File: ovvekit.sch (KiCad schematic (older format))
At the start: 29 parts, among them J1 ESP_PROG_JTAG, J2 ESP_PROG_UART, SW1 SW_Push, SW2 SW_Push, SW3 SW_Push, U1 ESP32-WROOM-32

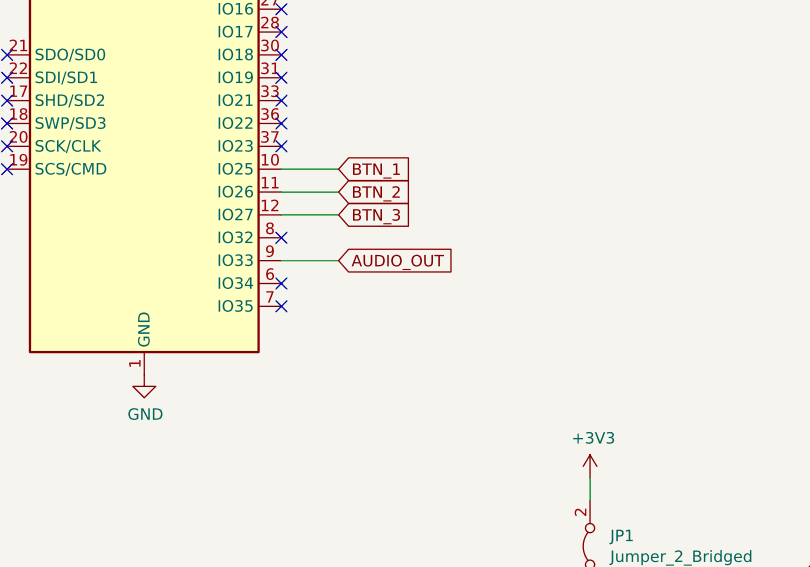
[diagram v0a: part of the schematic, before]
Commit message: Added a LDO, maybe not the final one but there is one on the PCB now. Added a voltage divider for measureing battery voltage.
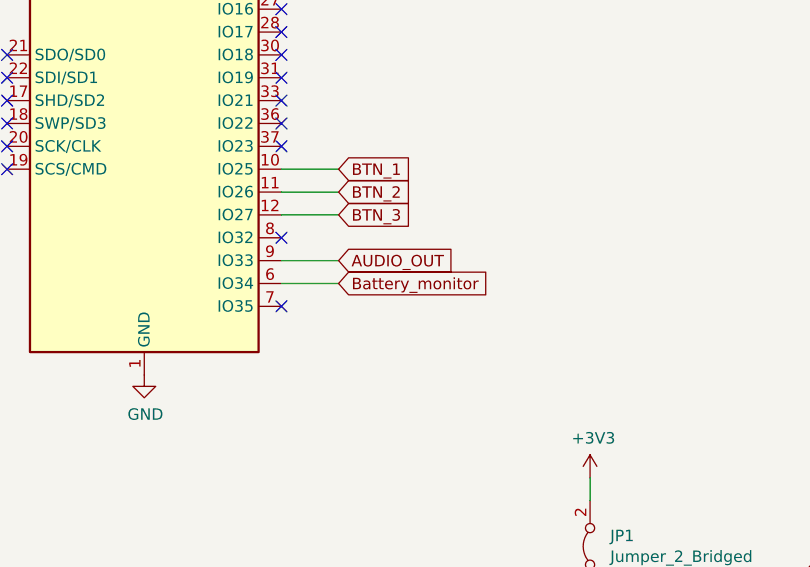
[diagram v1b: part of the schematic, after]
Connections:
- net Battery_monitor: now reaches U1.6 (IO34)
- no-connect marks 21 -> 20
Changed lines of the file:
@@
 Comment4 ""
 $EndDescr
-$Comp
-L RF_Module:ESP32-WROOM-32 U1
-U 1 1 6063995A
-P 4050 3200
-F 0 "U1" H 4050 4781 50  0000 C CNN
-F 1 "ESP32-WROOM-32" H 4050 4690 50  0000 C CNN
-F 2 "RF_Module:ESP32-WROOM-32" H 4050 1700 50  0001 C CNN
-F 3 "https://www.espressif.com/sites/default/files/documentation/esp32-wroom-32_datasheet_en.pdf" H 3750 3250 50  0001 C CNN
-	1    4050 3200
-	1    0    0    -1
-$EndComp
 Wire Wire Line
 	4900 3700 4650 3700
@@
 NoConn ~ 3450 3700
 NoConn ~ 4650 4300
-NoConn ~ 4650 4200
 NoConn ~ 4650 4000
 NoConn ~ 4650 3600
@@
 Wire Wire Line
 	6000 5150 6000 5050
+$Comp
+L RF_Module:ESP32-WROOM-32 U1
+U 1 1 6063995A
+P 4050 3200
+F 0 "U1" H 4050 4781 50  0000 C CNN
+F 1 "ESP32-WROOM-32" H 4050 4690 50  0000 C CNN
+F 2 "RF_Module:ESP32-WROOM-32" H 4050 1700 50  0001 C CNN
+F 3 "https://www.espressif.com/sites/default/files/documentation/esp32-wroom-32_datasheet_en.pdf" H 3750 3250 50  0001 C CNN
+	1    4050 3200
+	1    0    0    -1
+$EndComp
+Wire Wire Line
+	4900 4200 4650 4200
+Text GLabel 4900 4200 2    50   Input ~ 0
+Battery_monitor
 $EndSCHEMATC

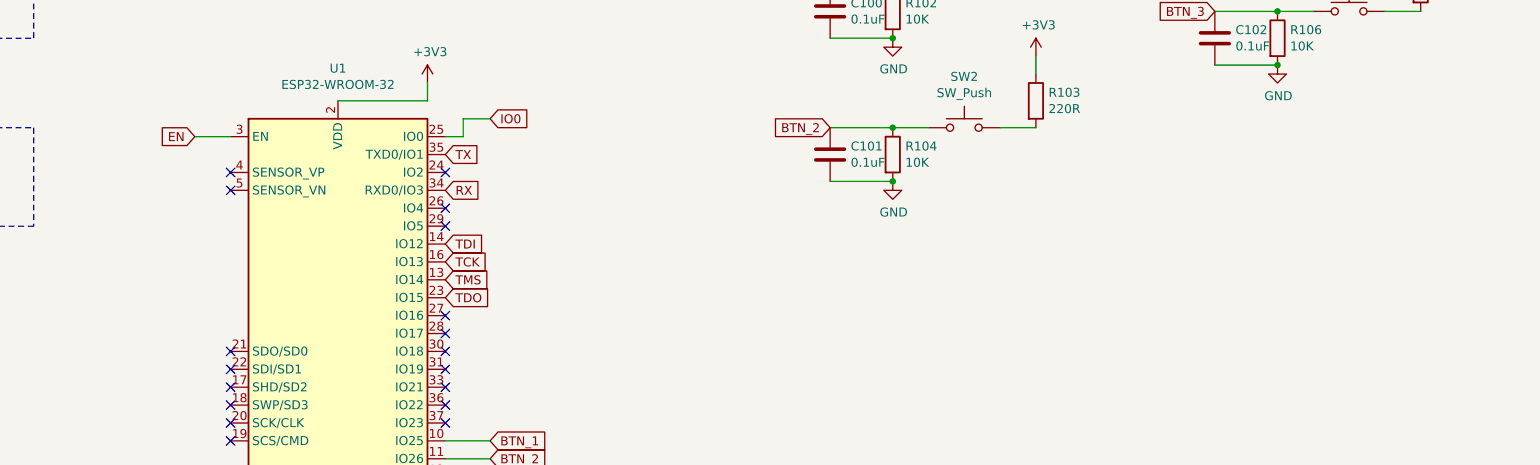
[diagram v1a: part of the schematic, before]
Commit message: Updated to kicad 6. Added AMS1117 regulator. Did more layout work in power section.
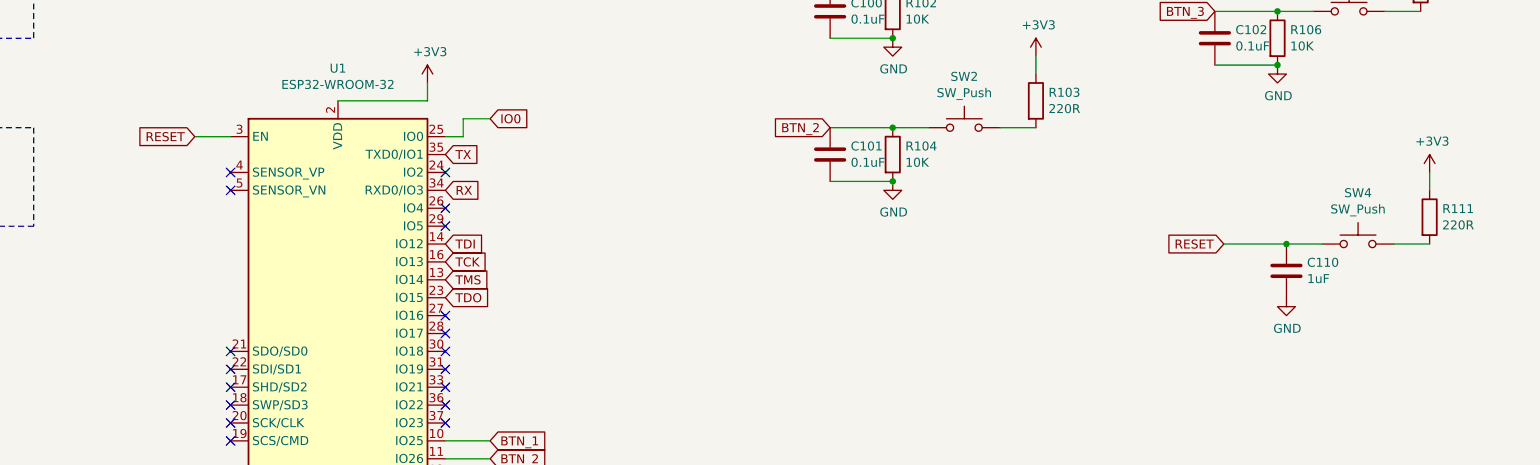
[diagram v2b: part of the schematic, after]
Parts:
- added C110: 1uF, Capacitor_SMD:C_0603_1608Metric, symbol Device:C
- added R111: 220R, Resistor_SMD:R_0603_1608Metric_Pad0.98x0.95mm_HandSolder, symbol Device:R
- added SW4: SW_Push, Button_Switch_SMD:SW_Push_1P1T_NO_6x6mm_H9.5mm, symbol Switch:SW_Push
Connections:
- net +3V3: now also R111.1
- net EN: no longer U1.3 (EN)
- net GND: now also C110.2
- new net: R111.2, SW4.2
- new net RESET: C110.1, SW4.1, U1.3 (EN)
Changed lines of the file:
@@
 RX
 Text GLabel 3250 2000 0    50   Input ~ 0
-EN
+RESET
 Text GLabel 4900 1900 2    50   Input ~ 0
 IO0
@@
 Text GLabel 4900 4200 2    50   Input ~ 0
 Battery_monitor
+$Comp
+L Switch:SW_Push SW4
+U 1 1 61B18AAF
+P 9750 2600
+F 0 "SW4" H 9750 2885 50  0000 C CNN
+F 1 "SW_Push" H 9750 2794 50  0000 C CNN
+F 2 "Button_Switch_SMD:SW_Push_1P1T_NO_6x6mm_H9.5mm" H 9750 2800 50  0001 C CNN
+F 3 "~" H 9750 2800 50  0001 C CNN
+	1    9750 2600
+	1    0    0    -1
+$EndComp
+$Comp
+L Device:R R111
+U 1 1 61B18AB5
+P 10150 2450
+F 0 "R111" H 10220 2496 50  0000 L CNN
+F 1 "220R" H 10220 2405 50  0000 L CNN
+F 2 "Resistor_SMD:R_0603_1608Metric_Pad0.98x0.95mm_HandSolder" V 10080 2450 50  0001 C CNN
+F 3 "~" H 10150 2450 50  0001 C CNN
+	1    10150 2450
+	1    0    0    -1
+$EndComp
+Wire Wire Line
+	9950 2600 10150 2600
+Text GLabel 9000 2600 0    50   Input ~ 0
+RESET
+$Comp
+L power:+3V3 #PWR0208
+U 1 1 61B18ABD
+P 10150 2200
+F 0 "#PWR0208" H 10150 2050 50  0001 C CNN
+F 1 "+3V3" H 10165 2373 50  0000 C CNN
+F 2 "" H 10150 2200 50  0001 C CNN
+F 3 "" H 10150 2200 50  0001 C CNN
+	1    10150 2200
+	1    0    0    -1
+$EndComp
+Wire Wire Line
+	10150 2300 10150 2200
+$Comp
+L power:GND #PWR0207
+U 1 1 61B18ACD
+P 9350 2900
+F 0 "#PWR0207" H 9350 2650 50  0001 C CNN
+F 1 "GND" H 9355 2727 50  0000 C CNN
+F 2 "" H 9350 2900 50  0001 C CNN
+F 3 "" H 9350 2900 50  0001 C CNN
+	1    9350 2900
+	1    0    0    -1
+$EndComp
+$Comp
+L Device:C C110
+U 1 1 61B18AD5
+P 9350 2750
+F 0 "C110" H 9465 2796 50  0000 L CNN
+F 1 "1uF" H 9465 2705 50  0000 L CNN
+F 2 "Capacitor_SMD:C_0603_1608Metric" H 9388 2600 50  0001 C CNN
+F 3 "~" H 9350 2750 50  0001 C CNN
+	1    9350 2750
+	1    0    0    -1
+$EndComp
+Wire Wire Line
+	9000 2600 9350 2600
+Connection ~ 9350 2600
+Wire Wire Line
+	9350 2600 9550 2600
 $EndSCHEMATC
